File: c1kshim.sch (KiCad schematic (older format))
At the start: 6 parts, among them J1 Conn_01x14, J11 Conn_02x20_Odd_Even, J12 Conn_02x06_Odd_Even, J2 Conn_01x14, J3 Conn_01x03, J4 Conn_01x02

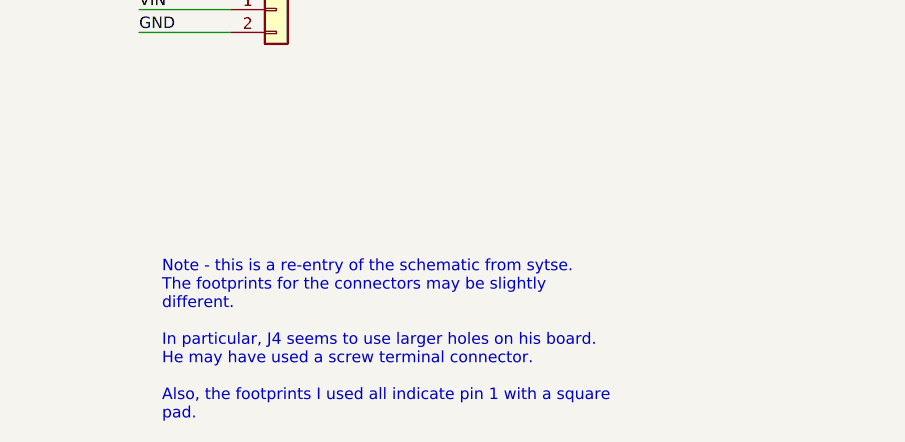
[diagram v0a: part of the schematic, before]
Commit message: Correct comments
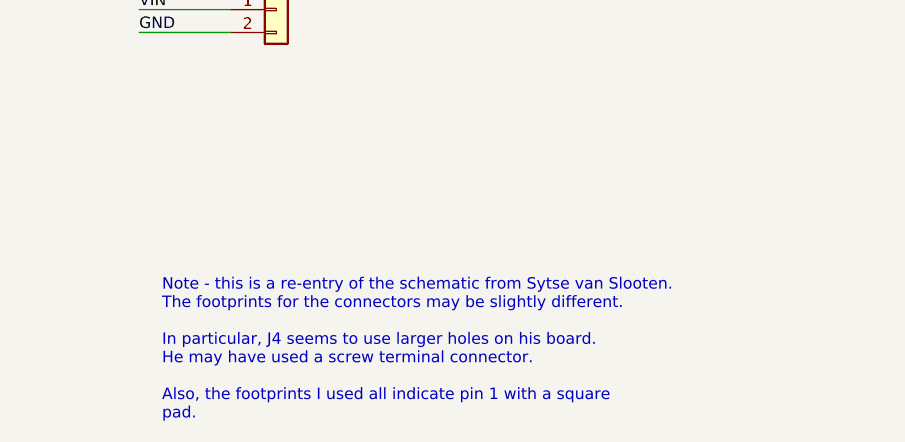
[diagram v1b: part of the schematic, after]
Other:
- note added: "Note - this is a re-entry of the schematic from Sytse van Slooten.\nThe footprints for the connectors may be slightly different.\n\nIn particular, J4 seems to use larger holes on his board.\nHe may have used a screw terminal connector.\n\nAlso, the footprints I used all indicate pin 1 with a square\npad."
- note removed: "Note - this is a re-entry of the schematic from sytse.\nThe footprints for the connectors may be slightly\ndifferent.\n\nIn particular, J4 seems to use larger holes on his board.\nHe may have used a screw terminal connector.\n\nAlso, the footprints I used all indicate pin 1 with a square\npad."
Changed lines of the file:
@@
 GND
 Text Notes 3800 7050 0    50   ~ 0
-Note - this is a re-entry of the schematic from sytse.\nThe footprints for the connectors may be slightly\ndifferent.\n\nIn particular, J4 seems to use larger holes on his board.\nHe may have used a screw terminal connector.\n\nAlso, the footprints I used all indicate pin 1 with a square\npad.
+Note - this is a re-entry of the schematic from Sytse van Slooten.\nThe footprints for the connectors may be slightly different.\n\nIn particular, J4 seems to use larger holes on his board.\nHe may have used a screw terminal connector.\n\nAlso, the footprints I used all indicate pin 1 with a square\npad.
 Text Label 3850 2400 2    50   ~ 0
 RESET
